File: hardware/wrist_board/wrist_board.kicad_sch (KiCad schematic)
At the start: 45 parts, among them J1 S2B-PH-K-S_LF__SN_, J2 USB_C_Receptacle_USB2.0_14P, J3 Conn_01x02, J4 Conn_01x02, J5 Conn_01x02, J6 Conn_01x02, J7 Conn_01x02, SW1 SW_SPST, U1 MCP73831T-2ACI_OT, U2 TLV75533PDBV, U3 MPU-6050, X1 ESP32-S3-WROOM-1-N16R8

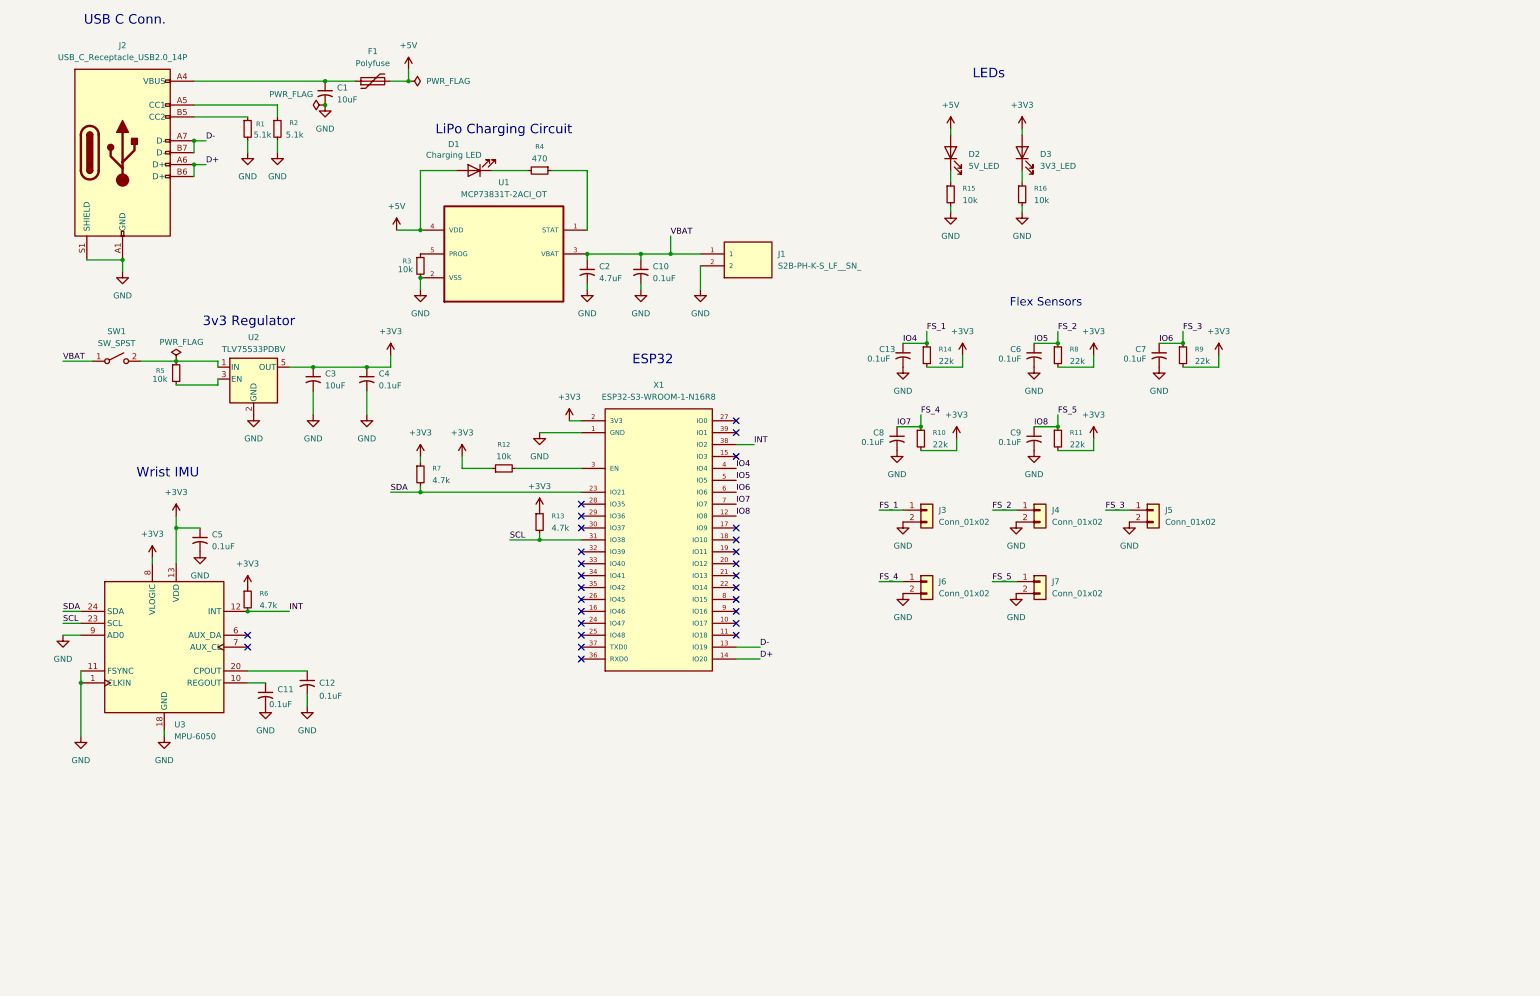
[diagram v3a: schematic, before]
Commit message: Added boot and reset buttons in schematic
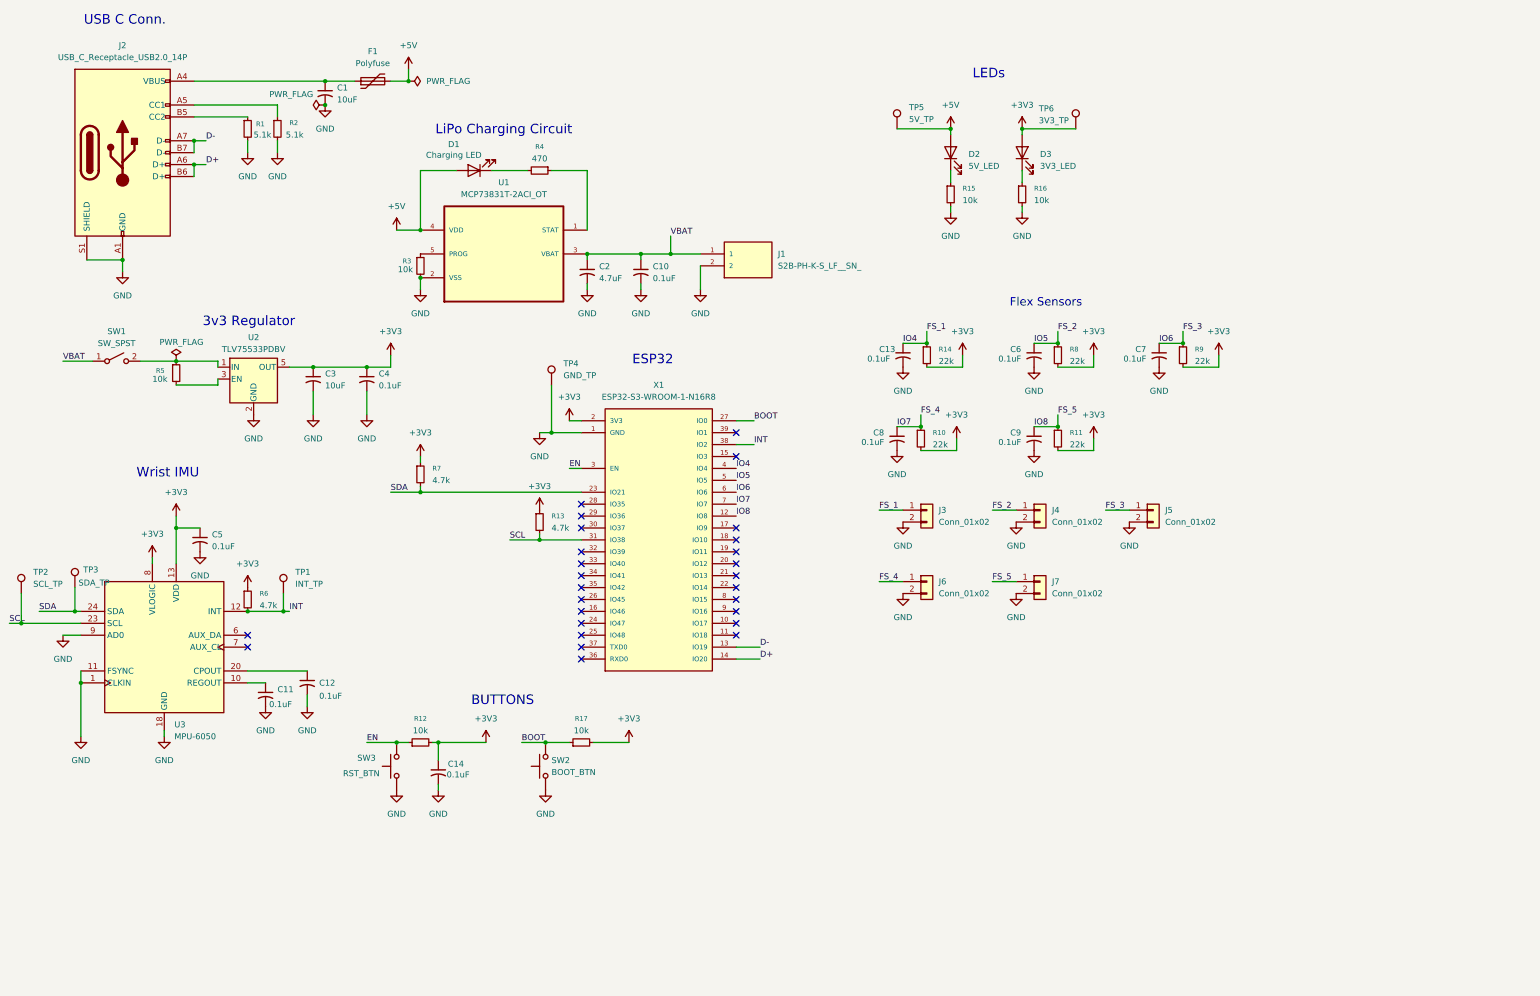
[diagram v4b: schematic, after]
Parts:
- added C14: 0.1uF, symbol Device:C_Small_US
- added R17: 10k, symbol Device:R_Small
- added SW2: BOOT_BTN, symbol Switch:SW_Push
- added SW3: RST_BTN, symbol Switch:SW_Push
- added TP1: INT_TP, symbol Connector:TestPoint
- added TP2: SCL_TP, symbol Connector:TestPoint
- added TP3: SDA_TP, symbol Connector:TestPoint
- added TP4: GND_TP, symbol Connector:TestPoint
- added TP5: 5V_TP, symbol Connector:TestPoint
- added TP6: 3V3_TP, symbol Connector:TestPoint
- R12: footprint Resistor_SMD:R_0805_2012Metric -> (none)
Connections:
- net +3V3: now also R12.2, C14.1, R17.2, TP6.1; no longer R12.1
- net +5V: now also TP5.1
- net GND: now also C14.2, SW2.1, SW3.1, TP4.1
- net INT: now also TP1.1
- net SCL: now also TP2.1
- net SDA: now also TP3.1
- net BOOT: now reaches X1.27 (IO0)
- net BOOT: now also R17.1, SW2.2
- net EN: now reaches X1.3 (EN)
- net EN: now also R12.1, SW3.2; no longer R12.2
- no-connect marks 28 -> 27
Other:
- note added: "BUTTONS"

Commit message: Added extra GPIO pinout
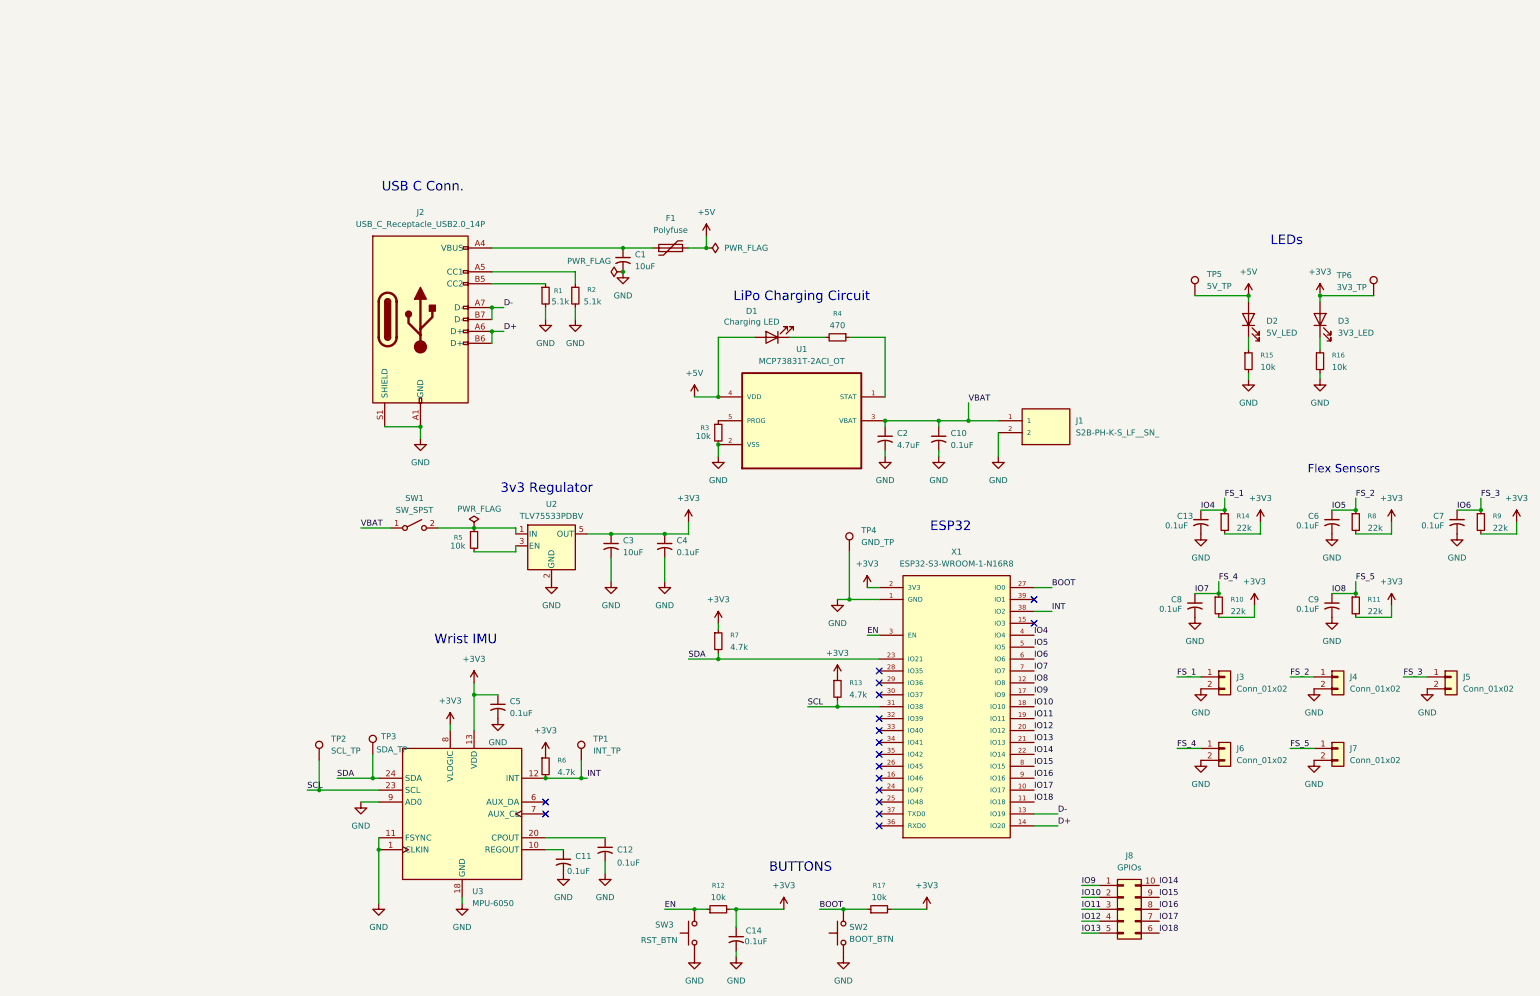
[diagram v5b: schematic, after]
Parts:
- added J8: GPIOs, Connector_PinHeader_2.54mm:PinHeader_2x05_P2.54mm_Vertical, symbol Connector_Generic:Conn_02x05_Counter_Clockwise
- C14: footprint (none) -> Capacitor_SMD:C_0805_2012Metric
- R12, R17: footprint (none) -> Resistor_SMD:R_0805_2012Metric
- SW2, SW3: footprint (none) -> Button_Switch_SMD:SW_SPST_B3U-1000P
- TP1, TP2, TP3, TP4, TP5, TP6: footprint (none) -> TestPoint:TestPoint_Loop_D2.60mm_Drill1.4mm_Beaded
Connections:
- net IO17: now reaches X1.10 (IO17)
- net IO17: now also J8.7 (Pin_7)
- net IO18: now reaches X1.11 (IO18)
- net IO18: now also J8.6 (Pin_6)
- net IO9: now reaches X1.17 (IO9)
- net IO9: now also J8.1 (Pin_1)
- net IO10: now reaches X1.18 (IO10)
- net IO10: now also J8.2 (Pin_2)
- net IO11: now reaches X1.19 (IO11)
- net IO11: now also J8.3 (Pin_3)
- net IO12: now reaches X1.20 (IO12)
- net IO12: now also J8.4 (Pin_4)
- net IO13: now reaches X1.21 (IO13)
- net IO13: now also J8.5 (Pin_5)
- net IO14: now reaches X1.22 (IO14)
- net IO14: now also J8.10 (Pin_10)
- net IO15: now reaches X1.8 (IO15)
- net IO15: now also J8.9 (Pin_9)
- net IO16: now reaches X1.9 (IO16)
- net IO16: now also J8.8 (Pin_8)
- no-connect marks 27 -> 17
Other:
- moved on the sheet: C1, C10, C11, C12, C13, C14, C2, C3, C4, C5, C6, C7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

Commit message: Added test points to layout
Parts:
- TP1, TP2, TP3, TP4, TP5, TP6: footprint TestPoint:TestPoint_Loop_D2.60mm_Drill1.4mm_Beaded -> TestPoint:TestPoint_Loop_D2.60mm_Drill0.9mm_Beaded
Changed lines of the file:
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@@
 			)
 		)
-		(property "Footprint" "TestPoint:TestPoint_Loop_D2.60mm_Drill1.4mm_Beaded"
+		(property "Footprint" "TestPoint:TestPoint_Loop_D2.60mm_Drill0.9mm_Beaded"
 			(at 271.78 80.01 0)
 			(effects
@@
 			)
 		)
-		(property "Footprint" "TestPoint:TestPoint_Loop_D2.60mm_Drill1.4mm_Beaded"
+		(property "Footprint" "TestPoint:TestPoint_Loop_D2.60mm_Drill0.9mm_Beaded"
 			(at 85.09 179.07 0)
 			(effects
@@
 			)
 		)
-		(property "Footprint" "TestPoint:TestPoint_Loop_D2.60mm_Drill1.4mm_Beaded"
+		(property "Footprint" "TestPoint:TestPoint_Loop_D2.60mm_Drill0.9mm_Beaded"
 			(at 309.88 80.01 0)
 			(effects
@@
 			)
 		)
-		(property "Footprint" "TestPoint:TestPoint_Loop_D2.60mm_Drill1.4mm_Beaded"
+		(property "Footprint" "TestPoint:TestPoint_Loop_D2.60mm_Drill0.9mm_Beaded"
 			(at 198.12 134.62 0)
 			(effects
@@
 			)
 		)
-		(property "Footprint" "TestPoint:TestPoint_Loop_D2.60mm_Drill1.4mm_Beaded"
+		(property "Footprint" "TestPoint:TestPoint_Loop_D2.60mm_Drill0.9mm_Beaded"
 			(at 96.52 177.8 0)
 			(effects
@@
 			)
 		)
-		(property "Footprint" "TestPoint:TestPoint_Loop_D2.60mm_Drill1.4mm_Beaded"
+		(property "Footprint" "TestPoint:TestPoint_Loop_D2.60mm_Drill0.9mm_Beaded"
 			(at 140.97 179.07 0)
 			(effects

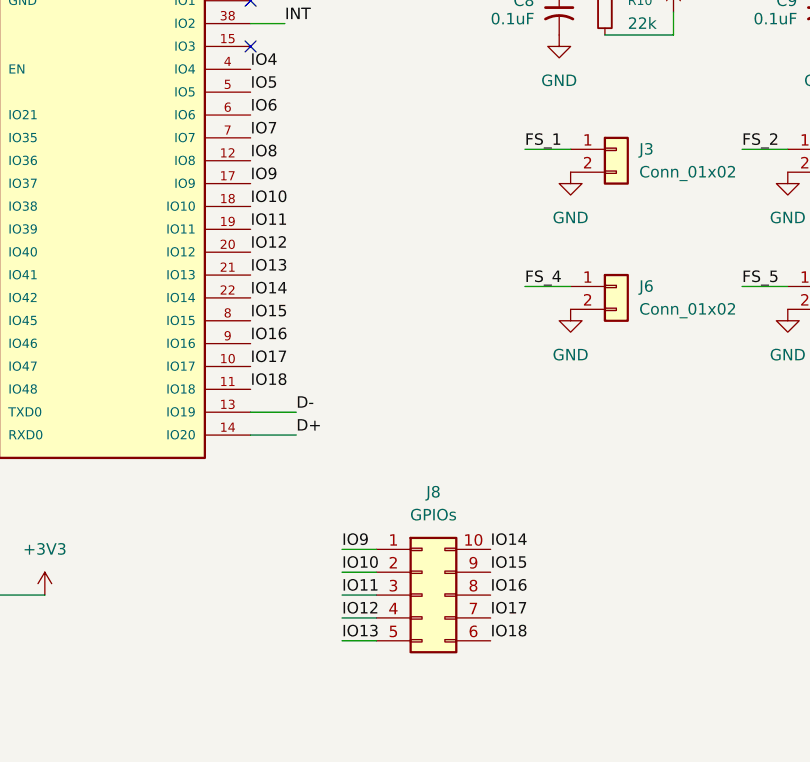
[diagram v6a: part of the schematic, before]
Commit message: Test points and extra GPIOs added to layout
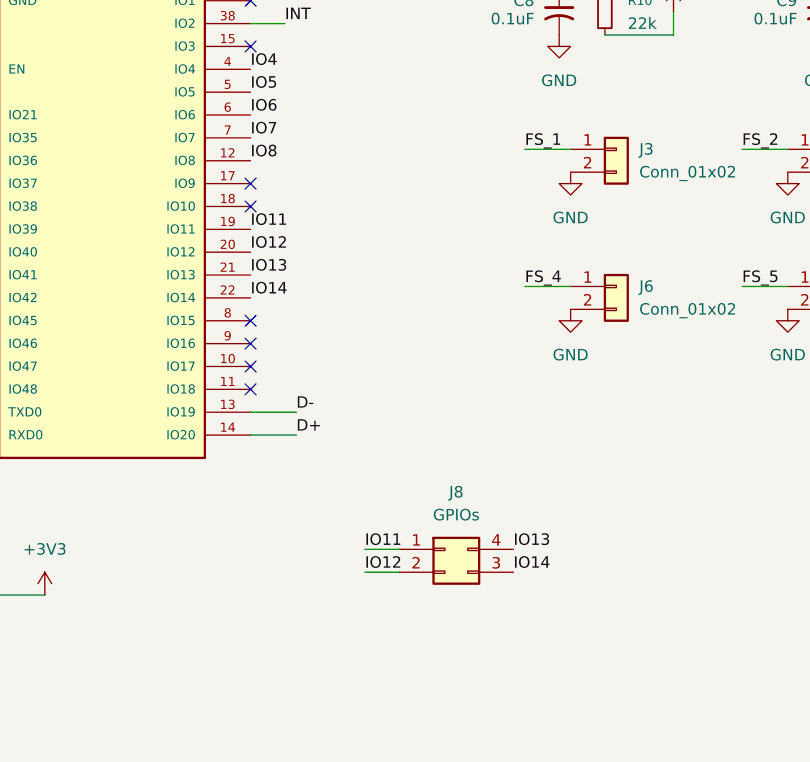
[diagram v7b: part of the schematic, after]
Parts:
- removed J8: GPIOs, Connector_PinHeader_2.54mm:PinHeader_2x05_P2.54mm_Vertical, symbol Connector_Generic:Conn_02x05_Counter_Clockwise
- added J8: GPIOs, Connector_PinHeader_2.54mm:PinHeader_2x02_P2.54mm_Vertical, symbol Connector_Generic:Conn_02x02_Counter_Clockwise
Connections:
- net IO11: now also J8.1 (Pin_1)
- net IO12: now also J8.2 (Pin_2)
- net IO13: now also J8.4 (Pin_4)
- net IO14: now also J8.3 (Pin_3)
- net IO10: no longer names the net of X1.18 (IO10)
- net IO15: no longer names the net of X1.8 (IO15)
- net IO16: no longer names the net of X1.9 (IO16)
- net IO17: no longer names the net of X1.10 (IO17)
- net IO18: no longer names the net of X1.11 (IO18)
- net IO9: no longer names the net of X1.17 (IO9)
- no-connect marks 17 -> 23

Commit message: Updates to wrist board for horizontal connections + mounting holes
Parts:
- J3, J4, J5, J6, J7: footprint Connector_PinHeader_2.54mm:PinHeader_1x02_P2.54mm_Vertical -> Connector_PinHeader_2.54mm:PinHeader_1x02_P2.54mm_Horizontal
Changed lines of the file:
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@@
 			)
 		)
-		(property "Footprint" "Connector_PinHeader_2.54mm:PinHeader_1x02_P2.54mm_Vertical"
+		(property "Footprint" "Connector_PinHeader_2.54mm:PinHeader_1x02_P2.54mm_Horizontal"
 			(at 297.18 161.29 0)
 			(effects
@@
 			)
 		)
-		(property "Footprint" "Connector_PinHeader_2.54mm:PinHeader_1x02_P2.54mm_Vertical"
+		(property "Footprint" "Connector_PinHeader_2.54mm:PinHeader_1x02_P2.54mm_Horizontal"
 			(at 297.18 176.53 0)
 			(effects
@@
 			)
 		)
-		(property "Footprint" "Connector_PinHeader_2.54mm:PinHeader_1x02_P2.54mm_Vertical"
+		(property "Footprint" "Connector_PinHeader_2.54mm:PinHeader_1x02_P2.54mm_Horizontal"
 			(at 273.05 176.53 0)
 			(effects
@@
 			)
 		)
-		(property "Footprint" "Connector_PinHeader_2.54mm:PinHeader_1x02_P2.54mm_Vertical"
+		(property "Footprint" "Connector_PinHeader_2.54mm:PinHeader_1x02_P2.54mm_Horizontal"
 			(at 273.05 161.29 0)
 			(effects
@@
 			)
 		)
-		(property "Footprint" "Connector_PinHeader_2.54mm:PinHeader_1x02_P2.54mm_Vertical"
+		(property "Footprint" "Connector_PinHeader_2.54mm:PinHeader_1x02_P2.54mm_Horizontal"
 			(at 321.31 161.29 0)
 			(effects
